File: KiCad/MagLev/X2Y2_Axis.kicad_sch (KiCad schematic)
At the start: 22 parts, among them Q1 2SD2673, Q2 2SB1708, Q3 2SD2673, Q4 2SB1708, U1 LM324

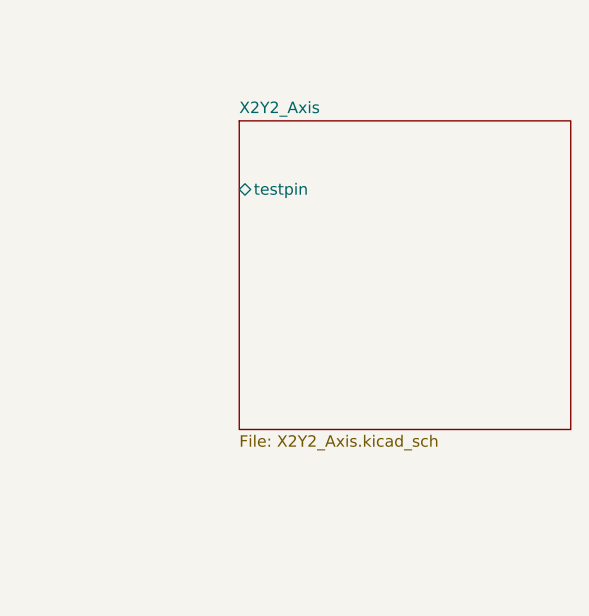
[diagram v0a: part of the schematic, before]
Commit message: Start schematic, add hierarchical sheet.
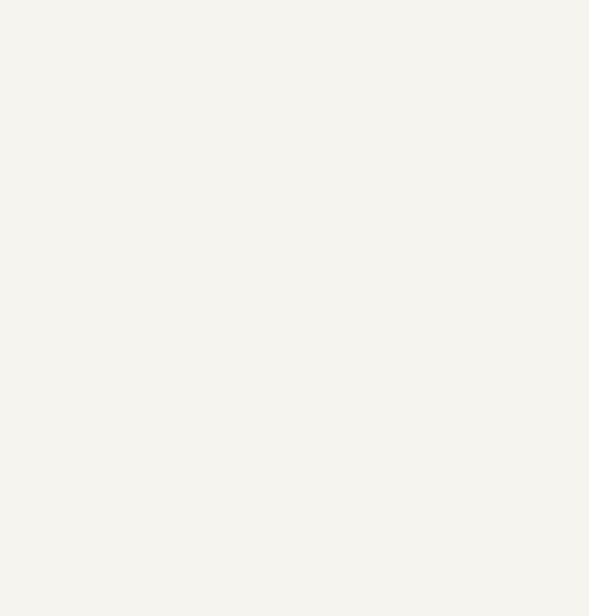
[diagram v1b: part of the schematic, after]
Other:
- removed sheet X2Y2_Axis
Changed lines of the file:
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@@
           (reference "R4") (unit 1)
         )
+        (path "/5eab7e8b-54e1-47d0-9dc3-1e7c3fa2f560/900c73f6-729e-4964-925d-c4d9cc6fa0a1"
+          (reference "R4") (unit 1)
+        )
       )
     )
@@
           (reference "Q4") (unit 1)
         )
+        (path "/5eab7e8b-54e1-47d0-9dc3-1e7c3fa2f560/900c73f6-729e-4964-925d-c4d9cc6fa0a1"
+          (reference "Q4") (unit 1)
+        )
       )
     )
@@
           (reference "R6") (unit 1)
         )
+        (path "/5eab7e8b-54e1-47d0-9dc3-1e7c3fa2f560/900c73f6-729e-4964-925d-c4d9cc6fa0a1"
+          (reference "R6") (unit 1)
+        )
       )
     )
@@
       (project "MagLev"
         (path "/5eab7e8b-54e1-47d0-9dc3-1e7c3fa2f560"
+          (reference "C1") (unit 1)
+        )
+        (path "/5eab7e8b-54e1-47d0-9dc3-1e7c3fa2f560/900c73f6-729e-4964-925d-c4d9cc6fa0a1"
           (reference "C1") (unit 1)
         )
@@
           (reference "U1") (unit 5)
         )
+        (path "/5eab7e8b-54e1-47d0-9dc3-1e7c3fa2f560/900c73f6-729e-4964-925d-c4d9cc6fa0a1"
+          (reference "U1") (unit 5)
+        )
       )
     )
@@
           (reference "U1") (unit 4)
         )
+        (path "/5eab7e8b-54e1-47d0-9dc3-1e7c3fa2f560/900c73f6-729e-4964-925d-c4d9cc6fa0a1"
+          (reference "U1") (unit 4)
+        )
       )
     )
@@
       (project "MagLev"
         (path "/5eab7e8b-54e1-47d0-9dc3-1e7c3fa2f560"
+          (reference "R2") (unit 1)
+        )
+        (path "/5eab7e8b-54e1-47d0-9dc3-1e7c3fa2f560/900c73f6-729e-4964-925d-c4d9cc6fa0a1"
           (reference "R2") (unit 1)
         )
@@
           (reference "U1") (unit 1)
         )
+        (path "/5eab7e8b-54e1-47d0-9dc3-1e7c3fa2f560/900c73f6-729e-4964-925d-c4d9cc6fa0a1"
+          (reference "U1") (unit 1)
+        )
       )
     )
@@
           (reference "L2") (unit 1)
         )
+        (path "/5eab7e8b-54e1-47d0-9dc3-1e7c3fa2f560/900c73f6-729e-4964-925d-c4d9cc6fa0a1"
+          (reference "L2") (unit 1)
+        )
       )
     )
@@
           (reference "R1") (unit 1)
         )
+        (path "/5eab7e8b-54e1-47d0-9dc3-1e7c3fa2f560/900c73f6-729e-4964-925d-c4d9cc6fa0a1"
+          (reference "R1") (unit 1)
+        )
       )
     )
@@
           (reference "#PWR01") (unit 1)
         )
+        (path "/5eab7e8b-54e1-47d0-9dc3-1e7c3fa2f560/900c73f6-729e-4964-925d-c4d9cc6fa0a1"
+          (reference "#PWR01") (unit 1)
+        )
       )
     )
@@
           (reference "D4") (unit 1)
         )
+        (path "/5eab7e8b-54e1-47d0-9dc3-1e7c3fa2f560/900c73f6-729e-4964-925d-c4d9cc6fa0a1"
+          (reference "D4") (unit 1)
+        )
       )
     )
@@
           (reference "L1") (unit 1)
         )
+        (path "/5eab7e8b-54e1-47d0-9dc3-1e7c3fa2f560/900c73f6-729e-4964-925d-c4d9cc6fa0a1"
+          (reference "L1") (unit 1)
+        )
       )
     )
@@
           (reference "R7") (unit 1)
         )
+        (path "/5eab7e8b-54e1-47d0-9dc3-1e7c3fa2f560/900c73f6-729e-4964-925d-c4d9cc6fa0a1"
+          (reference "R7") (unit 1)
+        )
       )
     )
@@
           (reference "Q2") (unit 1)
         )
+        (path "/5eab7e8b-54e1-47d0-9dc3-1e7c3fa2f560/900c73f6-729e-4964-925d-c4d9cc6fa0a1"
+          (reference "Q2") (unit 1)
+        )
       )
     )
@@
           (reference "R9") (unit 1)
         )
+        (path "/5eab7e8b-54e1-47d0-9dc3-1e7c3fa2f560/900c73f6-729e-4964-925d-c4d9cc6fa0a1"
+          (reference "R9") (unit 1)
+        )
       )
     )
@@
           (reference "#PWR02") (unit 1)
         )
+        (path "/5eab7e8b-54e1-47d0-9dc3-1e7c3fa2f560/900c73f6-729e-4964-925d-c4d9cc6fa0a1"
+          (reference "#PWR02") (unit 1)
+        )
       )
     )
@@
           (reference "R3") (unit 1)
         )
+        (path "/5eab7e8b-54e1-47d0-9dc3-1e7c3fa2f560/900c73f6-729e-4964-925d-c4d9cc6fa0a1"
+          (reference "R3") (unit 1)
+        )
       )
     )
@@
           (reference "D1") (unit 1)
         )
+        (path "/5eab7e8b-54e1-47d0-9dc3-1e7c3fa2f560/900c73f6-729e-4964-925d-c4d9cc6fa0a1"
+          (reference "D1") (unit 1)
+        )
       )
     )
@@
           (reference "#PWR03") (unit 1)
         )
+        (path "/5eab7e8b-54e1-47d0-9dc3-1e7c3fa2f560/900c73f6-729e-4964-925d-c4d9cc6fa0a1"
+          (reference "#PWR03") (unit 1)
+        )
       )
     )
@@
       (project "MagLev"
         (path "/5eab7e8b-54e1-47d0-9dc3-1e7c3fa2f560"
+          (reference "D2") (unit 1)
+        )
+        (path "/5eab7e8b-54e1-47d0-9dc3-1e7c3fa2f560/900c73f6-729e-4964-925d-c4d9cc6fa0a1"
           (reference "D2") (unit 1)
         )
@@
           (reference "U1") (unit 3)
         )
+        (path "/5eab7e8b-54e1-47d0-9dc3-1e7c3fa2f560/900c73f6-729e-4964-925d-c4d9cc6fa0a1"
+          (reference "U1") (unit 3)
+        )
       )
     )
@@
           (reference "Q3") (unit 1)
         )
+        (path "/5eab7e8b-54e1-47d0-9dc3-1e7c3fa2f560/900c73f6-729e-4964-925d-c4d9cc6fa0a1"
+          (reference "Q3") (unit 1)
+        )
       )
     )
@@
           (reference "R5") (unit 1)
         )
+        (path "/5eab7e8b-54e1-47d0-9dc3-1e7c3fa2f560/900c73f6-729e-4964-925d-c4d9cc6fa0a1"
+          (reference "R5") (unit 1)
+        )
       )
     )
@@
           (reference "D3") (unit 1)
         )
+        (path "/5eab7e8b-54e1-47d0-9dc3-1e7c3fa2f560/900c73f6-729e-4964-925d-c4d9cc6fa0a1"
+          (reference "D3") (unit 1)
+        )
       )
     )
@@
           (reference "R8") (unit 1)
         )
+        (path "/5eab7e8b-54e1-47d0-9dc3-1e7c3fa2f560/900c73f6-729e-4964-925d-c4d9cc6fa0a1"
+          (reference "R8") (unit 1)
+        )
       )
     )
@@
       (project "MagLev"
         (path "/5eab7e8b-54e1-47d0-9dc3-1e7c3fa2f560"
+          (reference "R10") (unit 1)
+        )
+        (path "/5eab7e8b-54e1-47d0-9dc3-1e7c3fa2f560/900c73f6-729e-4964-925d-c4d9cc6fa0a1"
           (reference "R10") (unit 1)
         )
@@
           (reference "U1") (unit 2)
         )
+        (path "/5eab7e8b-54e1-47d0-9dc3-1e7c3fa2f560/900c73f6-729e-4964-925d-c4d9cc6fa0a1"
+          (reference "U1") (unit 2)
+        )
       )
     )
@@
           (reference "Q1") (unit 1)
         )
-      )
-    )
-  )
-  (sheet (at 195.58 43.18) (size 36.83 34.29) (fields_autoplaced)
-    (stroke (width 0.1524) (type solid))
-    (fill (color 0 0 0 0.0000))
-    (property "Sheetname" "X2Y2_Axis" (at 195.58 42.4684 0)
-      (effects (font (size 1.27 1.27)) (justify left bottom))
-    )
-    (property "Sheetfile" "X2Y2_Axis.kicad_sch" (at 195.58 78.0546 0)
-      (effects (font (size 1.27 1.27)) (justify left top))
-    )
-    (pin "testpin" bidirectional (at 195.58 50.8 180)
-      (effects (font (size 1.27 1.27)) (justify left))
-    )
-    (instances
-      (project "MagLev"
-        (path "/5eab7e8b-54e1-47d0-9dc3-1e7c3fa2f560" (page "2"))
-      )
-    )
-  )
-  (sheet_instances
-    (path "/" (page "1"))
+        (path "/5eab7e8b-54e1-47d0-9dc3-1e7c3fa2f560/900c73f6-729e-4964-925d-c4d9cc6fa0a1"
+          (reference "Q1") (unit 1)
+        )
+      )
+    )
   )
 )
